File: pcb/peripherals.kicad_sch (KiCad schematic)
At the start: 39 parts, among them J4 Conn_01x03, J5 Conn_01x03, J6 Conn_01x03, J7 Conn_01x03, Q7 BSS138, Q8 AO3407A, SW10 GENERAL, SW4 SW_DIP_x04, SW7 GENERAL, SW8 GENERAL, SW9 GENERAL, U14 PCF8563T, U15 PCA9555PW, Y2 32.768kHz 9pF

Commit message: Add U4 decoupling cap, source U15 MPN, improve GND/GNDREF visual distinction
- Add local decoupling capacitor to U4 (74LVC1G08) VCC/GND
- Add missing Manf/MPN/LCSC Part# to U15 (PCA9555PWR, TI, C2864778) found
  during a full net-trace design review
- Color all GNDREF net wires in battery_18650_input.kicad_sch orange to
  make the intentional GND/GNDREF current-sense split (bridged only by
  R13) visually obvious on the canvas, not just from the net name
- Add a schematic text note at R13 documenting the split for reviewers
  without access to CLAUDE.md

Co-Authored-By: Claude Sonnet 5 <noreply@anthropic.com>
Claude-Session: https://claude.ai/code/session_01LhLkuH6sQ5GbUZ61bG7p2h
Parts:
- U15: LCSC Part # (none) -> C2864778; MPN (none) -> PCA9555PWR; Manf (none) -> TI
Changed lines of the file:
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@@
+			)
+		)
+		(property "Manf" "TI"
+			(at 207.01 46.99 0)
+			(hide yes)
+			(show_name no)
+			(do_not_autoplace no)
+			(effects
+				(font
+					(size 1.27 1.27)
+				)
+			)
+		)
+		(property "MPN" "PCA9555PWR"
+			(at 207.01 46.99 0)
+			(hide yes)
+			(show_name no)
+			(do_not_autoplace no)
+			(effects
+				(font
+					(size 1.27 1.27)
+				)
+			)
+		)
+		(property "LCSC Part #" "C2864778"
+			(at 207.01 46.99 0)
+			(hide yes)
+			(show_name no)
+			(do_not_autoplace no)
+			(effects
+				(font
+					(size 1.27 1.27)
+				)
 			)
 		)

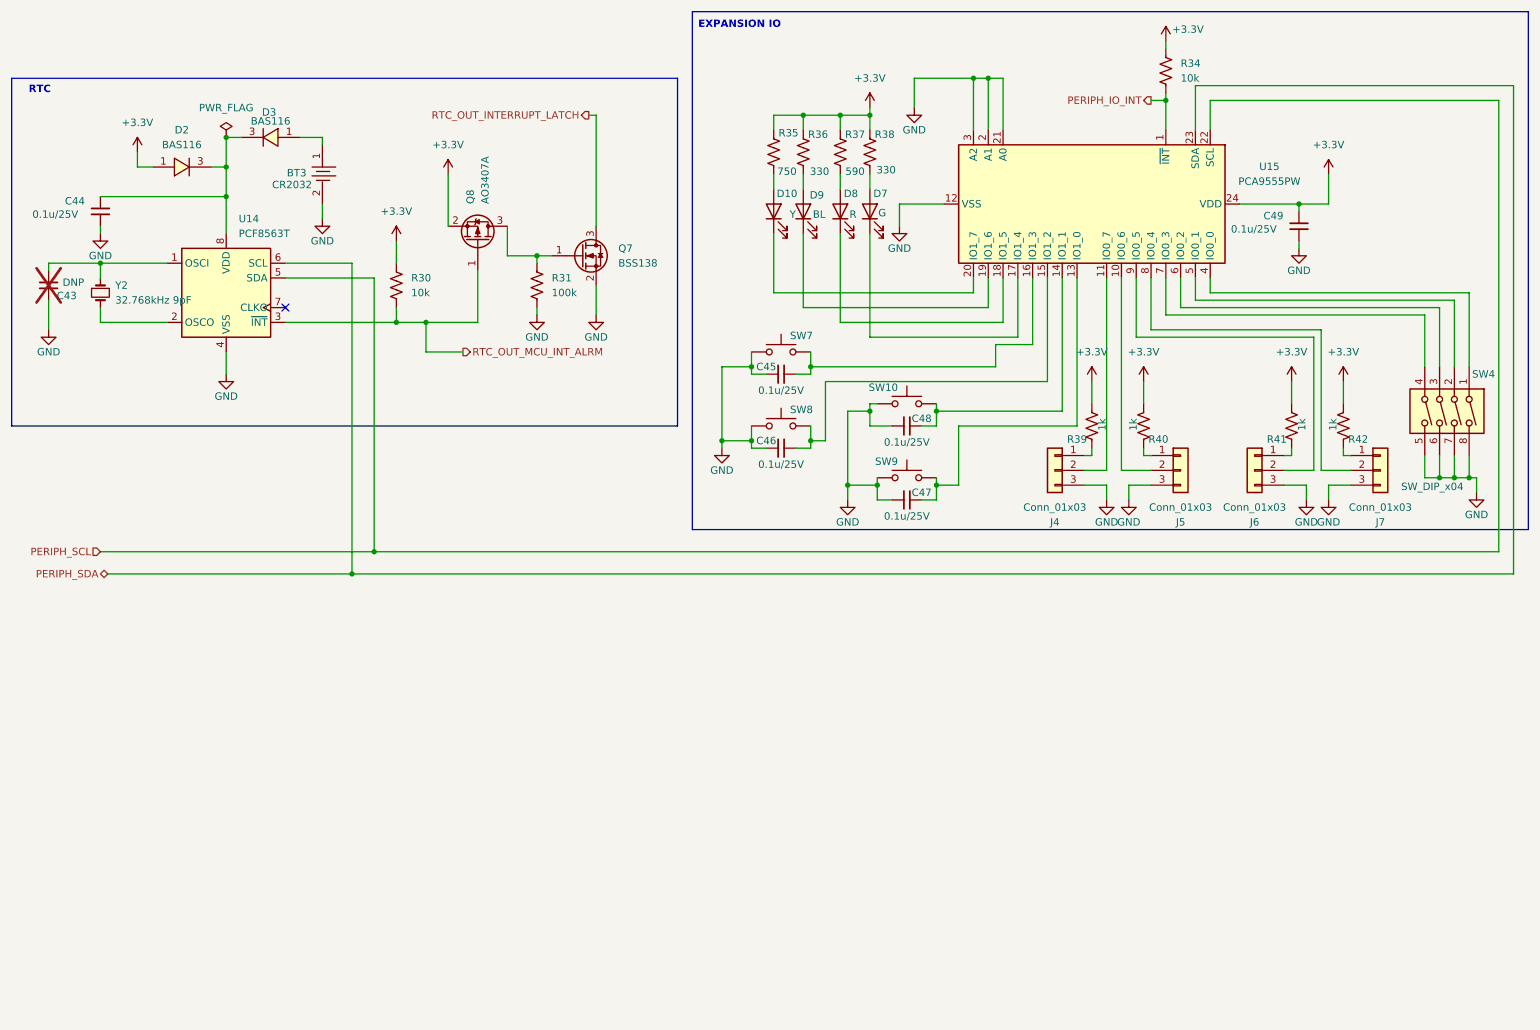
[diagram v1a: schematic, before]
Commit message: Wire SD card interface, fix R29/Q6/Q7 sourcing, localize datasheets project-wide
- SD card (Card1, Molex 472192001) wired to the FSPI (SPI2) peripheral:
  IO10/FSPICS0->CS, IO11/FSPID->MOSI, IO12/FSPICLK->SCLK, IO13/FSPIQ->MISO;
  shield/mounting tabs renamed SHLD and grounded; local decoupling cap added
- R29 was silently a 10k YAGEO part (RC0603FR-0710KL/C98220) sitting under a
  1M designator -- corrected to the real 1M part (RC0603FR-071ML/C105578),
  matching this rail's documented VRAW soft-latch bleed design intent
- Q6, Q7 (BSS138): added missing Manf/MPN/LCSC Part# (onsemi BSS138LT1G,
  C82045)
- C32/C36: normalized Value strings; fixed C36's Datasheet, which pointed to
  a different capacitor's PDF entirely
- Localized every remaining component's Datasheet field to a project-local
  path across all 8 schematic sheets (was a live remote URL before), per
  the new datasheet-localization task; caught and rejected a wrong-language
  and a wrong-manufacturer-clone source along the way (U8, U14, U15, Y2)
- Fixed 4 datasheet fields (Q1, D1, U6, U7) that had reverted from their
  already-localized paths back to remote URLs, apparently from a native
  KiCad symbol-library resync picking up stale library-level defaults

Co-Authored-By: Claude Sonnet 5 <noreply@anthropic.com>
Claude-Session: https://claude.ai/code/session_01LhLkuH6sQ5GbUZ61bG7p2h
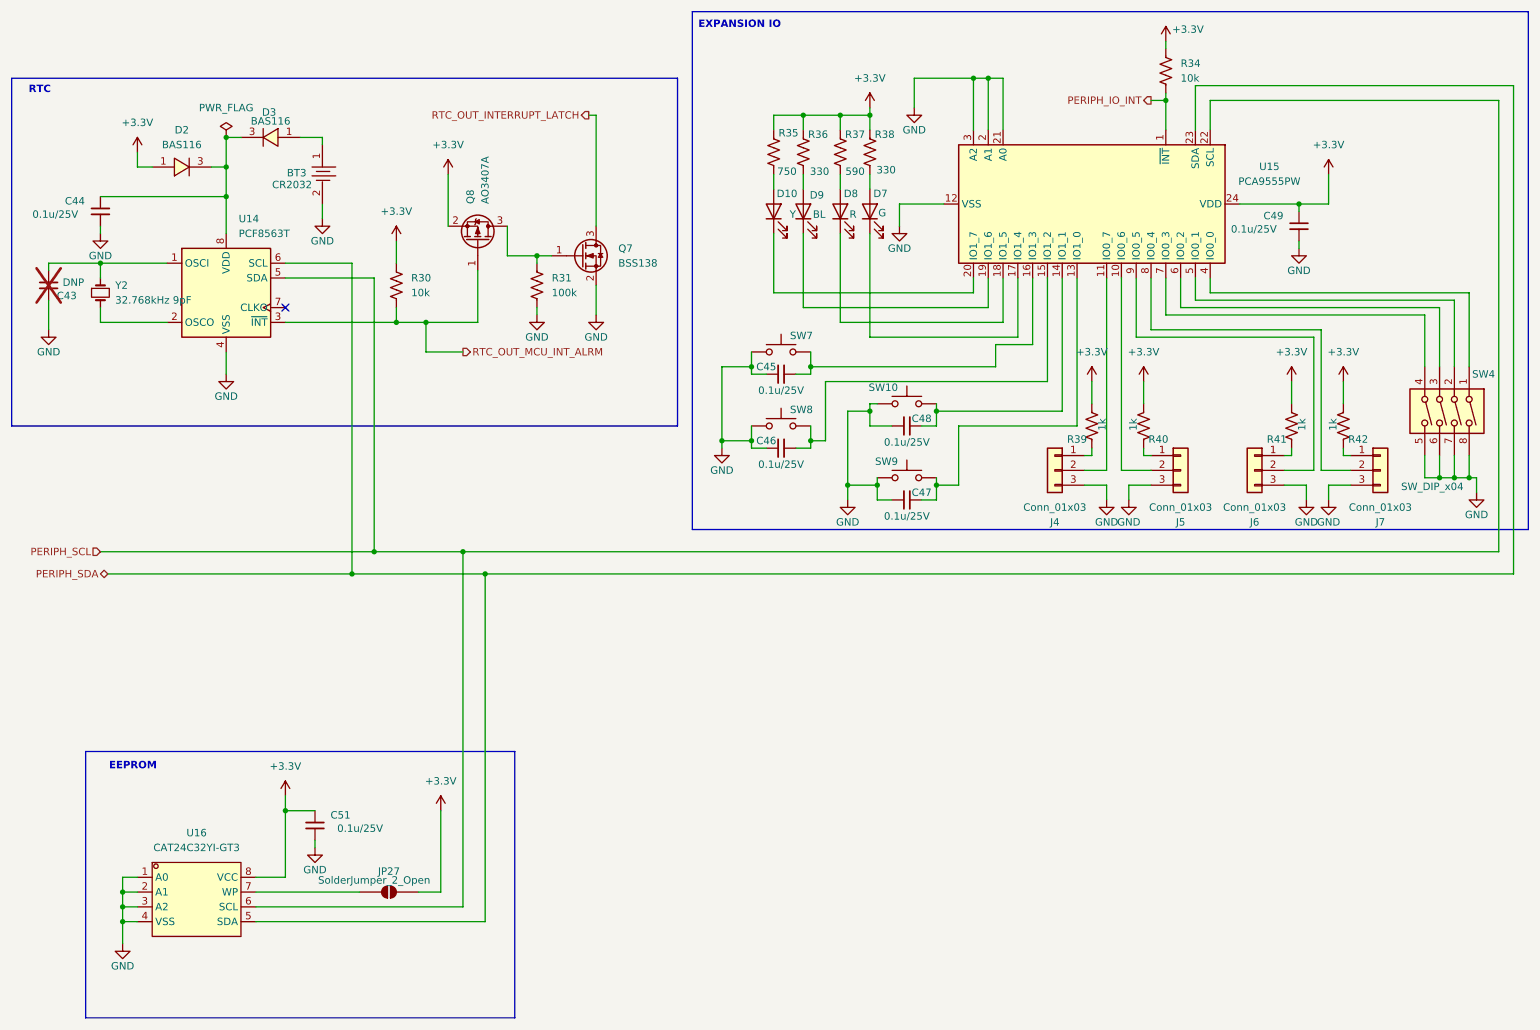
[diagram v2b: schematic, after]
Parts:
- added C51: 0.1u/25V, Capacitor_SMD:C_0603_1608Metric, symbol Device:C_Small
- added JP27: SolderJumper_2_Open, Jumper:SolderJumper-2_P1.3mm_Open_TrianglePad1.0x1.5mm, symbol Jumper:SolderJumper_2_Open
- added U16: CAT24C32YI-GT3, kicad_gx_library:TSSOP-8_L4.4-W3.0-P0.65-LS6.4-BL, symbol kicad_gx_library:CAT24C32YI-GT3
- BT3: LCSC Part # (none) -> C964787; Manf (none) -> MYOUNG(美阳)
- Y2: footprint Crystal:Crystal_SMD_3215-2Pin_3.2x1.5mm -> Crystal:Crystal_SMD_5032-2Pin_5.0x3.2mm; PROD_ID (none) -> XTAL-
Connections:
- net +3.3V: now also C51.1, JP27.2 (B), U16.8 (VCC)
- net GND: now also C51.2, U16.1 (A0), U16.2 (A1), U16.3 (A2), U16.4 (VSS)
- net PERIPH_SCL: now also U16.6 (SCL)
- net PERIPH_SDA: now also U16.5 (SDA)
- new net: JP27.1 (A), U16.7 (WP)
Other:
- note added: "EEPROM"

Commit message: Fix remaining mass-symbol-update reversions (67 Datasheet + 5 Footprint fields)
The project-wide "Update Symbols from Library" run reverted far more than
the 4 caught in the previous commit -- most of that commit's own claimed
"localized project-wide" state was actually already the reverted state,
since the mass update happened before that commit and git history alone
couldn't detect it. Cross-referenced every component's Datasheet/Footprint
against the independent tracking docs (project_library_datasheets.md,
kicad_gx_library_datasheets.md, footprint_verification_log.md) instead.

- 67 components: Datasheet reverted from a localized ${KIPRJMOD} path back
  to a remote URL, across all 8 schematic files
- 5 components: Footprint also reverted, not just Datasheet -- Y2 (RTC
  crystal) reverted to a physically different package size (5.0x3.2mm vs.
  the real 3.2x1.5mm part); U9/U12 (LM1117 LDOs), U10 (ESP32-S3 module),
  and Y1 (12MHz crystal) reverted to differently-sourced but plausible
  footprints from a vendored library instead of the verified stock ones

No MPN/Manf/LCSC Part#/Value regressions found (checked all 185
components). ERC clean, same 15 pre-existing errors as before.

Co-Authored-By: Claude Sonnet 5 <noreply@anthropic.com>
Claude-Session: https://claude.ai/code/session_01LhLkuH6sQ5GbUZ61bG7p2h
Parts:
- Y2: footprint Crystal:Crystal_SMD_5032-2Pin_5.0x3.2mm -> Crystal:Crystal_SMD_3215-2Pin_3.2x1.5mm
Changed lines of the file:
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@@
 			)
 		)
-		(property "Footprint" "Crystal:Crystal_SMD_5032-2Pin_5.0x3.2mm"
+		(property "Footprint" "Crystal:Crystal_SMD_3215-2Pin_3.2x1.5mm"
 			(at 29.21 62.23 0)
 			(hide yes)
@@
 			)
 		)
-		(property "Datasheet" "https://www.lcsc.com/datasheet/C519280.pdf"
+		(property "Datasheet" "${KIPRJMOD}/project_library/datasheets/NDK/NX3215SA-32.768K-STD-MUA-9.pdf"
 			(at 31.75 62.23 0)
 			(hide yes)
@@
 			)
 		)
-		(property "Datasheet" "https://www.lcsc.com/datasheet/C83916.pdf"
+		(property "Datasheet" "${KIPRJMOD}/project_library/datasheets/Korean_Hroparts_Elec/K2-1102SP-A4SC-04.pdf"
 			(at 175.26 88.9 0)
 			(hide yes)
@@
 			)
 		)
-		(property "Datasheet" "https://www.lcsc.com/datasheet/C5366382.pdf"
+		(property "Datasheet" "${KIPRJMOD}/project_library/datasheets/Kingbright/APTD2012LSURCK.pdf"
 			(at 163.83 48.26 0)
 			(hide yes)
@@
 			)
 		)
-		(property "Datasheet" "https://www.lcsc.com/datasheet/C319050.pdf"
+		(property "Datasheet" "${KIPRJMOD}/project_library/datasheets/XKB_Connection/DSHP04TS-S.pdf"
 			(at 266.7 82.55 0)
 			(hide yes)
@@
 			)
 		)
-		(property "Datasheet" "https://www.lcsc.com/datasheet/C22548.pdf"
+		(property "Datasheet" "${KIPRJMOD}/project_library/datasheets/YAGEO/RC0603FR-071KL.pdf"
 			(at 241.3 85.09 0)
 			(hide yes)
@@
 			)
 		)
-		(property "Datasheet" "https://www.lcsc.com/datasheet/C83916.pdf"
+		(property "Datasheet" "${KIPRJMOD}/project_library/datasheets/Korean_Hroparts_Elec/K2-1102SP-A4SC-04.pdf"
 			(at 153.67 80.01 0)
 			(hide yes)
@@
 			)
 		)
-		(property "Datasheet" "https://www.lcsc.com/datasheet/C160353.pdf"
+		(property "Datasheet" "${KIPRJMOD}/project_library/datasheets/JST/B3B-PH-SM4-TB_LF__SN_.pdf"
 			(at 234.95 92.71 0)
 			(hide yes)
@@
 			)
 		)
-		(property "Datasheet" "https://www.lcsc.com/datasheet/C95204.pdf"
+		(property "Datasheet" "${KIPRJMOD}/project_library/datasheets/YAGEO/RT0603BRD0710KL.pdf"
 			(at 219.71 24.13 0)
 			(hide yes)
@@
 			)
 		)
-		(property "Datasheet" "http://www.aosmd.com/pdfs/datasheet/AO3401A.pdf"
+		(property "Datasheet" "${KIPRJMOD}/project_library/datasheets/AOS/AO3407A.pdf"
 			(at 97.79 48.26 0)
 			(hide yes)
@@
 			)
 		)
-		(property "Datasheet" "https://www.lcsc.com/datasheet/C22548.pdf"
+		(property "Datasheet" "${KIPRJMOD}/project_library/datasheets/YAGEO/RC0603FR-071KL.pdf"
 			(at 207.01 85.09 0)
 			(hide yes)
@@
 			)
 		)
-		(property "Datasheet" "https://www.lcsc.com/datasheet/C859077.pdf"
+		(property "Datasheet" "${KIPRJMOD}/project_library/datasheets/YAGEO/RC0603DR-07590RL.pdf"
 			(at 163.83 38.1 0)
 			(hide yes)
@@
 			)
 		)
-		(property "Datasheet" "https://www.lcsc.com/datasheet/C160353.pdf"
+		(property "Datasheet" "${KIPRJMOD}/project_library/datasheets/JST/B3B-PH-SM4-TB_LF__SN_.pdf"
 			(at 256.54 92.71 0)
 			(hide yes)
@@
 			)
 		)
-		(property "Datasheet" "https://www.lcsc.com/datasheet/C105881.pdf"
+		(property "Datasheet" "${KIPRJMOD}/project_library/datasheets/YAGEO/RC0603FR-07330RL.pdf"
 			(at 157.48 38.1 0)
 			(hide yes)
@@
 			)
 		)
-		(property "Datasheet" "https://www.lcsc.com/datasheet/C5569446.pdf"
+		(property "Datasheet" "${KIPRJMOD}/project_library/datasheets/Kingbright/APT2012LZGCK.pdf"
 			(at 168.91 48.26 0)
 			(hide yes)
@@
 			)
 		)
-		(property "Datasheet" "https://www.lcsc.com/datasheet/C160353.pdf"
+		(property "Datasheet" "${KIPRJMOD}/project_library/datasheets/JST/B3B-PH-SM4-TB_LF__SN_.pdf"
 			(at 222.25 92.71 0)
 			(hide yes)
@@
 			)
 		)
-		(property "Datasheet" "https://www.lcsc.com/datasheet/C105881.pdf"
+		(property "Datasheet" "${KIPRJMOD}/project_library/datasheets/YAGEO/RC0603FR-07330RL.pdf"
 			(at 168.91 38.1 0)
 			(hide yes)
@@
 			)
 		)
-		(property "Datasheet" "https://www.lcsc.com/datasheet/C114635.pdf"
+		(property "Datasheet" "${KIPRJMOD}/project_library/datasheets/YAGEO/RC0603FR-07750RL.pdf"
 			(at 152.4 38.1 0)
 			(hide yes)
@@
 			)
 		)
-		(property "Datasheet" "https://www.nxp.com/docs/en/data-sheet/PCA9555.pdf"
+		(property "Datasheet" "${KIPRJMOD}/project_library/datasheets/TI/PCA9555PWR.pdf"
 			(at 207.01 46.99 0)
 			(hide yes)
@@
 			)
 		)
-		(property "Datasheet" "https://www.lcsc.com/datasheet/C22548.pdf"
+		(property "Datasheet" "${KIPRJMOD}/project_library/datasheets/YAGEO/RC0603FR-071KL.pdf"
 			(at 215.9 85.09 0)
 			(hide yes)
@@
 			)
 		)
-		(property "Datasheet" "https://www.lcsc.com/datasheet/C5588998.pdf"
+		(property "Datasheet" "${KIPRJMOD}/project_library/datasheets/Kingbright/APTD2012LSYCK.pdf"
 			(at 152.4 48.26 0)
 			(hide yes)
@@
 			)
 		)
-		(property "Datasheet" "https://www.lcsc.com/datasheet/C22548.pdf"
+		(property "Datasheet" "${KIPRJMOD}/project_library/datasheets/YAGEO/RC0603FR-071KL.pdf"
 			(at 250.19 85.09 0)
 			(hide yes)
@@
 			)
 		)
-		(property "Datasheet" "https://www.lcsc.com/datasheet/C95204.pdf"
+		(property "Datasheet" "${KIPRJMOD}/project_library/datasheets/YAGEO/RT0603BRD0710KL.pdf"
 			(at 87.63 60.96 0)
 			(hide yes)
@@
 			)
 		)
-		(property "Datasheet" "https://www.lcsc.com/datasheet/C83916.pdf"
+		(property "Datasheet" "${KIPRJMOD}/project_library/datasheets/Korean_Hroparts_Elec/K2-1102SP-A4SC-04.pdf"
 			(at 175.26 76.2 0)
 			(hide yes)
@@
 			)
 		)
-		(property "Datasheet" "https://www.lcsc.com/datasheet/C5879058.pdf"
+		(property "Datasheet" "${KIPRJMOD}/project_library/datasheets/Kingbright/APTD2012LQBC_D.pdf"
 			(at 157.48 48.26 0)
 			(hide yes)
@@
 			)
 		)
-		(property "Datasheet" "https://www.lcsc.com/datasheet/C83916.pdf"
+		(property "Datasheet" "${KIPRJMOD}/project_library/datasheets/Korean_Hroparts_Elec/K2-1102SP-A4SC-04.pdf"
 			(at 153.67 67.31 0)
 			(hide yes)
@@
 			)
 		)
-		(property "Datasheet" "https://www.lcsc.com/datasheet/C14675.pdf"
+		(property "Datasheet" "${KIPRJMOD}/project_library/datasheets/YAGEO/RC0603FR-07100KL.pdf"
 			(at 111.76 60.96 0)
 			(hide yes)
@@
 			)
 		)
-		(property "Datasheet" "https://www.lcsc.com/datasheet/C160353.pdf"
+		(property "Datasheet" "${KIPRJMOD}/project_library/datasheets/JST/B3B-PH-SM4-TB_LF__SN_.pdf"
 			(at 200.66 92.71 0)
 			(hide yes)
@@
 			)
 		)
-		(property "Datasheet" "https://www.nxp.com/docs/en/data-sheet/PCF8563.pdf"
+		(property "Datasheet" "${KIPRJMOD}/project_library/datasheets/NXP/PCF8563T_5_518.pdf"
 			(at 58.42 62.23 0)
 			(hide yes)
